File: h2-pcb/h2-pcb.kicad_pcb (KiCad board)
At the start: 2 copper layers, 123 x 75 mm, 102 parts, among them J1 Network Connector, J10 Temp Sensor Conn 3, J11 Actuator Connector 4, J12 Manometer Connector 3, J2 STDC14, J3 Manometer Connector 1, J4 Manometer Connector 2, J5 Actuator Connector 1, J6 Actuator Connector 2, J7 Actuator Connector 3, J8 Temp Sensor Conn 1, J9 Temp Sensor Conn 2, Q1 NMOS, Q2 PMOS, Q3 NMOS, Q4 PMOS, Q5 NMOS, Q6 PMOS, Q7 NMOS, Q8 PMOS, SW1 SW_Push, U1 LD39050PU33R, U2 STM32G474RBT6, U3 SN65HVD230, U4 DS2484R, Y1 8MHz

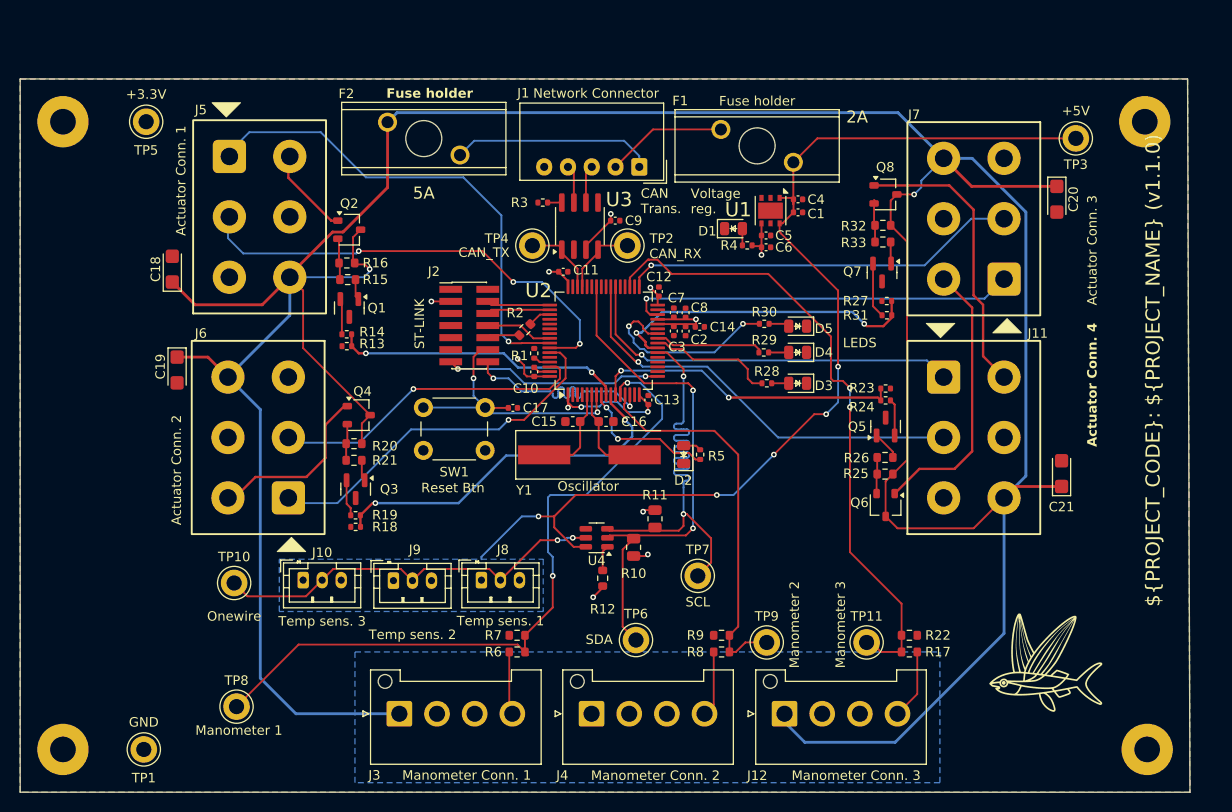
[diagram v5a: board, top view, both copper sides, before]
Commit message: h2-pcb: add plane for left actuator connectors
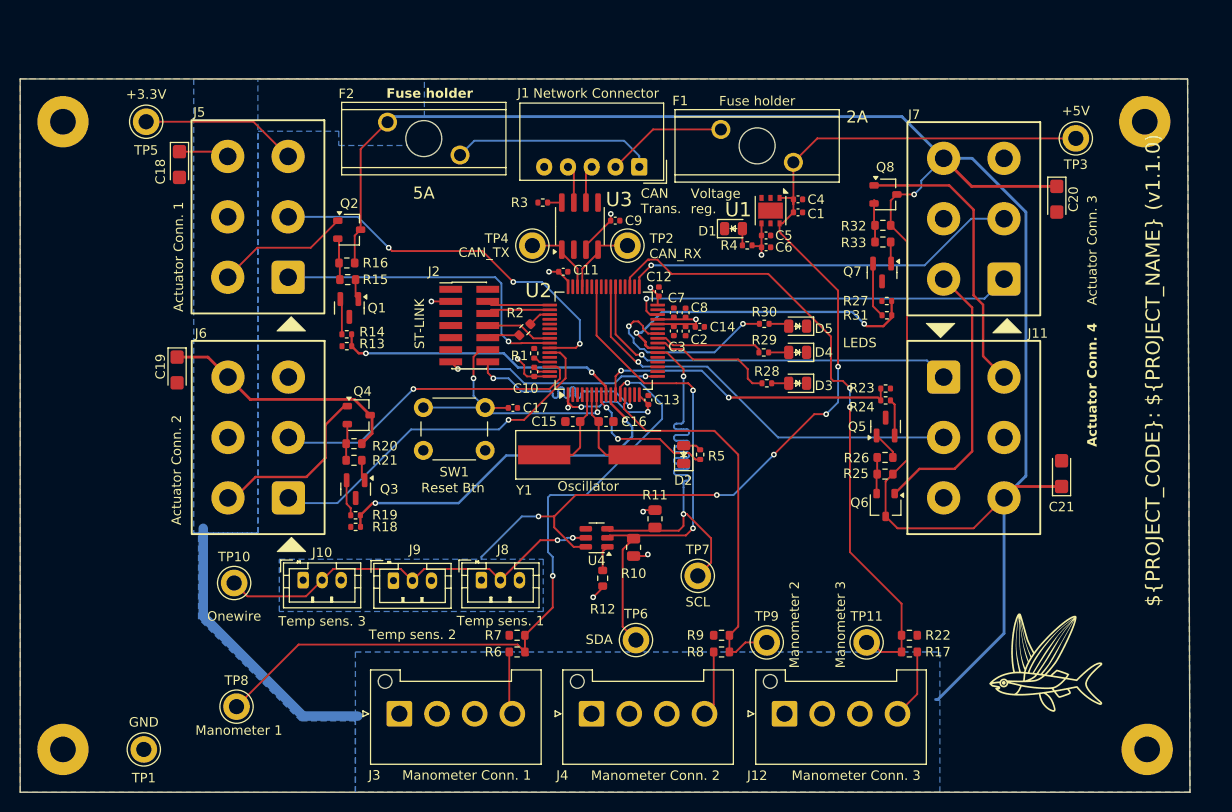
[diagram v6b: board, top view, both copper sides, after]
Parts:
- moved C18 11.0 mm to (56.8, 57.8), turned to -90 degrees
- moved J5 0.17 mm to (65.0, 63.2), turned to -90 degrees
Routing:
- net +24V: track 364.5 -> 283.8 mm, vias 2 -> 1
- net /NO_1: track 51.5 -> 33.8 mm
- net +3.3V: track 48.0 -> 63.7 mm
- net /NC_1: track 48.9 -> 41.0 mm
- net /ACTUATOR_CTRL1: track 9.37 -> 15.0 mm

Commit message: h2-pcb: Add 24V zone for connectors, change footprint for temp sensors + connect
Made 24V zone for right actuators connectors, network connector and 24V fuse holder.
Changed the temperature sensor connectors to JST_PH_S3B-PH-k_1x03_P2.00mm_Horizontal and placed them on the left side of pcb.
Followed with connecting the temperature sensors on the pcb.
TODO : fix 5 errors in DRC.
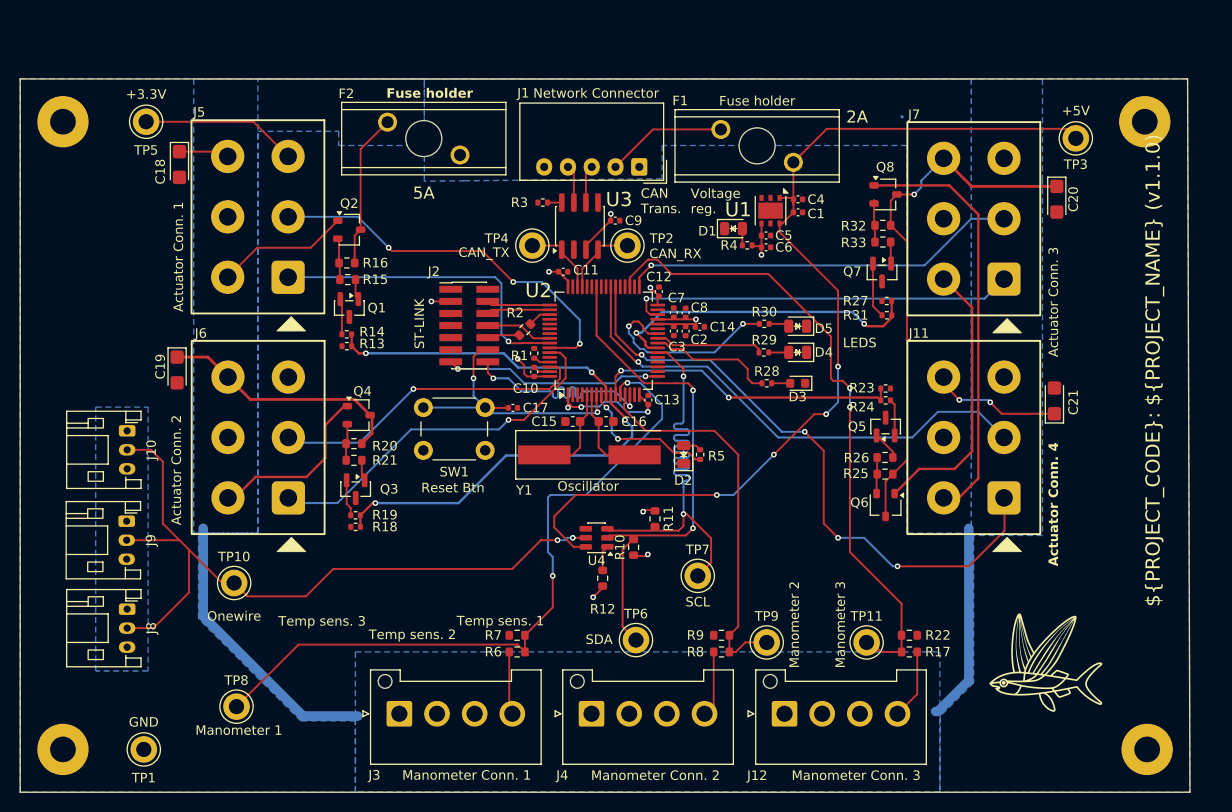
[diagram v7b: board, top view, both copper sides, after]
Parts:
- D3: footprint Exocet:LED_0805_2012Metric_With_Annotations -> LED_SMD:LED_0603_1608Metric
- J10: value Temp Sensor Conn 3 -> Temp Sens Conn 3; footprint Connector_JST:JST_PH_B3B-PH-K_1x03_P2.00mm_Vertical -> Connector_JST:JST_PH_S3B-PH-K_1x03_P2.00mm_Horizontal
- J8: value Temp Sensor Conn 1 -> Temp Sens Conn 1; footprint Connector_JST:JST_PH_B3B-PH-K_1x03_P2.00mm_Vertical -> Connector_JST:JST_PH_S3B-PH-K_1x03_P2.00mm_Horizontal
- J9: footprint Connector_JST:JST_PH_B3B-PH-K_1x03_P2.00mm_Vertical -> Connector_JST:JST_PH_S3B-PH-K_1x03_P2.00mm_Horizontal
- R10, R11: value 5.6k -> 6.8k; footprint Resistor_SMD:R_0805_2012Metric -> Resistor_SMD:R_0603_1608Metric
- R12: value 2.2 k -> 6.8k
- moved J8 37.4 mm to (51.2, 104.5), turned to -90 degrees
- moved J9 28.7 mm to (51.2, 95.2), turned to -90 degrees
- moved J10 24.3 mm to (51.2, 85.8), turned to -90 degrees
- moved C21 7.68 mm to (148.8, 82.6)
- turned J11 to -90 degrees
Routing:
- net +24V: track 283.8 -> 171.5 mm, vias 1 -> 3
- net /ONEWIRE: track 42.1 -> 79.4 mm
- net /NO_4: track 41.4 -> 67.0 mm, vias 1 -> 4
- net Net-(J1-+24V): track 21.3 -> 0.00 mm
- net /ACTUATOR_CTRL4: track 30.4 -> 44.5 mm
- net +5V: track 111.7 -> 102.3 mm, vias 5 -> 4
- net /NC_4: track 44.7 -> 53.3 mm

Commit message: h2-pcb: Fix DRC errors
Rotated the right actuator connectors and moved the zones to include the 3.3V zone with the rest of its zone. Added a zone for the Net J1 24V.
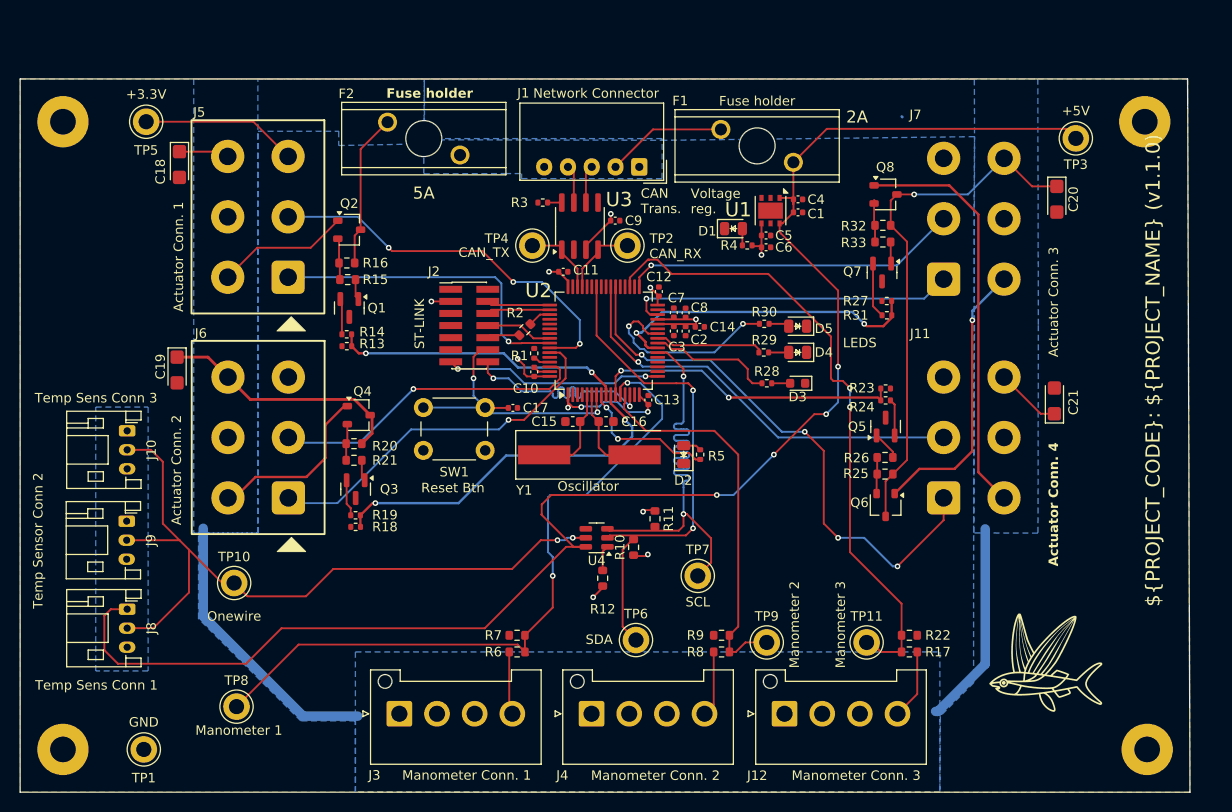
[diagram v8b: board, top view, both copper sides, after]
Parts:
- J11, J7: moved to B.Cu
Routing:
- net +5V: track 102.3 -> 167.6 mm
- net /NC_4: track 53.3 -> 44.7 mm
- net /NO_4: track 67.0 -> 59.6 mm
- net /NO_3: track 41.1 -> 34.7 mm
- net /NC_3: track 41.9 -> 35.6 mm
- net +24V: track 171.5 -> 165.5 mm, vias 3 -> 1
- net /ACTUATOR_CTRL4: track 44.5 -> 43.5 mm
- net +3.3V: track 63.7 -> 64.4 mm
- net /ACTUATOR_CTRL3: track 29.3 -> 29.5 mm, vias 0 -> 1
- added copper zone on B.Cu, net Net-(J1-+24V)
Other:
- board text added: "Temp Sens Conn 1"
- board text added: "Temp Sens Conn 3"
- board text added: "Temp Sensor Conn 2"
- board text removed: "Temp sens. 1"
- board text removed: "Temp sens. 2"
- board text removed: "Temp sens. 3"
